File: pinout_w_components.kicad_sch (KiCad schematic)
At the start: 40 parts, among them J1 10155435-00011LF, U10 ESDS304DBVR, U11 ESD351DPYR, U12 TJA1051TK-3, U9 ESDS304DBVR

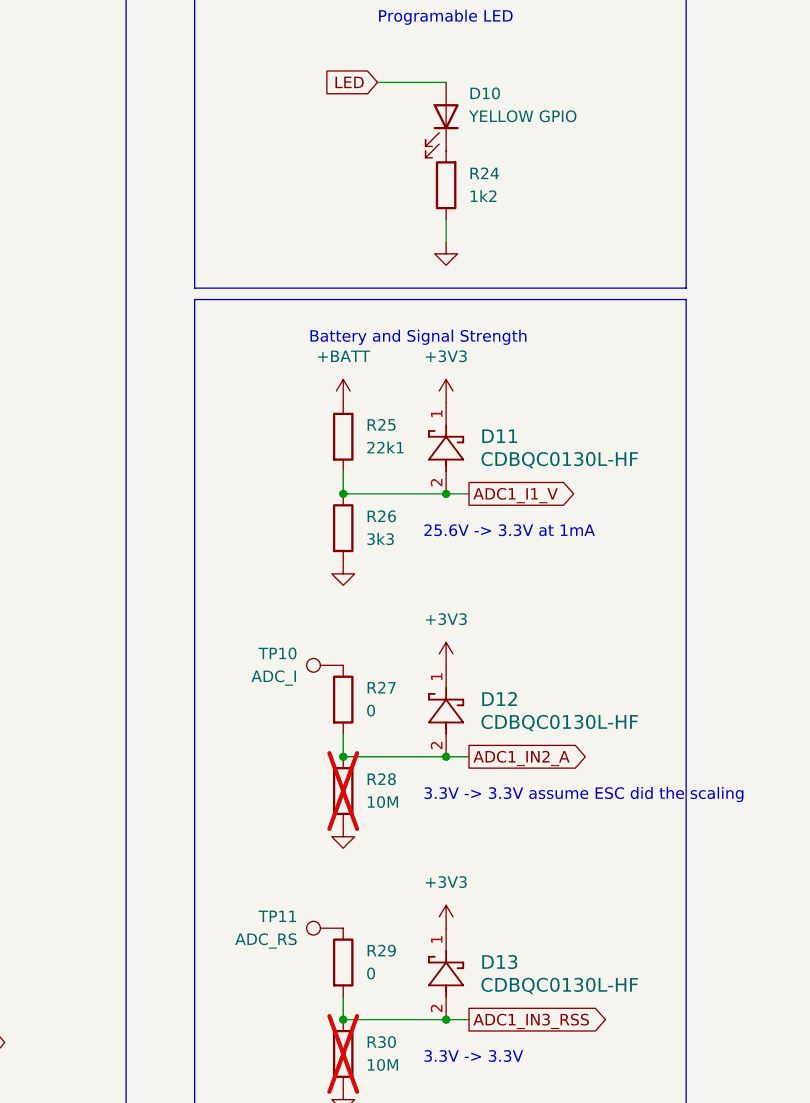
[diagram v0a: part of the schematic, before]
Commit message: replace flash memory with SD flash memory; move SPI2 terminations closer to source
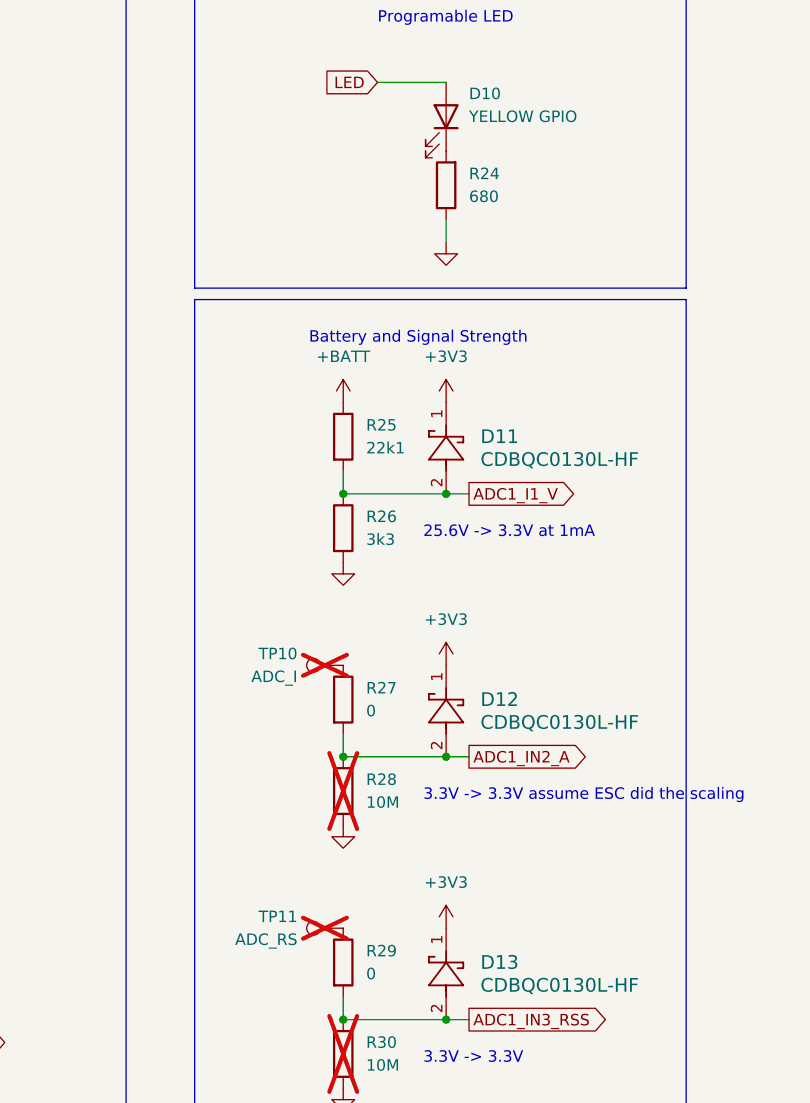
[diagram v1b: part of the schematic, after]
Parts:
- C40, C41: Part Number CC0402KRX7R7BB104 -> CC0402KRX5R8BB104; Voltage 16 -> 25
- C42: Manufactorer YAGEO -> Murata; Part Number CC0402JRX7R9BB472 -> GRM155R61H472KA01D; Voltage 16 -> 50
- C43, C44: Part Number CC0402JRX7R7BB101 -> CC0402JRNPO9BN101; Voltage 16 -> 50
- C51: Part Number GRM188C71C225KE11D -> GRM188R61E225KA12D; Voltage 16 -> 25
- R24: value 1k2 -> 680; Part Number RC0402FR-071K2L -> RC0402FR-07680RP
- R27: Part Number RP0402BRD0722K1L -> RC0402FR-070RL
- R28: Note (none) -> DNP; Part Number RT0402BRD073K3L -> RC0402JR-0710ML
- R29: Part Number RT0402BRD073K3L -> RC0402FR-070RL
- R30: Note (none) -> DNP
- TP10, TP11: now not fitted
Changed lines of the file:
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@@
 			)
 		)
-		(property "Part Number" "RT0402BRD073K3L"
+		(property "Part Number" "RC0402JR-0710ML"
+			(at 119.38 153.67 0)
+			(effects
+				(font
+					(size 1.27 1.27)
+				)
+				(hide yes)
+			)
+		)
+		(property "Note" "DNP"
 			(at 119.38 153.67 0)
 			(effects
@@
 			)
 		)
-		(property "Datasheet" "ESD351DPYR"
+		(property "Datasheet" "https://www.ti.com/general/docs/suppproductinfo.tsp?distId=10&gotoUrl=https%3A%2F%2Fwww.ti.com%2Flit%2Fgpn%2Fesd351"
 			(at 41.91 190.5 0)
 			(effects
@@
 			)
 		)
-		(property "Datasheet" "CDBQC0130L-HF"
+		(property "Datasheet" "https://www.comchiptech.com/admin/files/product/CDBQC0130L-HF%20RevB681116.pdf"
 			(at 130.81 179.07 0)
 			(effects
@@
 			)
 		)
-		(property "Part Number" "CC0402KRX7R7BB104"
+		(property "Part Number" "CC0402KRX5R8BB104"
 			(at 163.83 48.26 0)
 			(effects
@@
 			)
 		)
-		(property "Voltage" "16"
+		(property "Voltage" "25"
 			(at 163.83 48.26 0)
 			(effects
@@
 			)
 		)
-		(property "Part Number" "CC0402KRX7R7BB104"
+		(property "Part Number" "CC0402KRX5R8BB104"
 			(at 220.98 27.94 0)
 			(effects
@@
 			)
 		)
-		(property "Voltage" "16"
+		(property "Voltage" "25"
 			(at 220.98 27.94 0)
 			(effects
@@
 			)
 		)
-		(property "Part Number" "RP0402BRD0722K1L"
+		(property "Part Number" "RC0402FR-070RL"
 			(at 119.38 143.51 0)
 			(effects
@@
 			)
 		)
-		(property "Datasheet" "ESDS304DBVR"
+		(property "Datasheet" "https://www.ti.com/lit/ds/symlink/esds302.pdf?HQS=dis-dk-null-digikeymode-dsf-pf-null-wwe&ts=1721661223795&ref_url=https%253A%252F%252Ficqqg.com%252F"
 			(at 48.26 135.89 0)
 			(effects
@@
 			)
 		)
-		(property "Datasheet" "ESDS304DBVR"
+		(property "Datasheet" "https://www.ti.com/lit/ds/symlink/esds302.pdf?HQS=dis-dk-null-digikeymode-dsf-pf-null-wwe&ts=1721661223795&ref_url=https%253A%252F%252Ficqqg.com%252F"
 			(at 48.26 54.61 0)
 			(effects
@@
 			)
 		)
-		(property "Part Number" "CC0402JRX7R7BB101"
+		(property "Part Number" "CC0402JRNPO9BN101"
 			(at 209.55 50.8 0)
 			(effects
@@
 			)
 		)
-		(property "Voltage" "16"
+		(property "Voltage" "50"
 			(at 209.55 50.8 0)
 			(effects
@@
 			)
 		)
+		(property "Note" "DNP"
+			(at 119.38 182.88 0)
+			(effects
+				(font
+					(size 1.27 1.27)
+				)
+				(hide yes)
+			)
+		)
 		(pin "1"
 		)
@@
 			)
 		)
-		(property "Datasheet" "CDBQC0130L-HF"
+		(property "Datasheet" "https://www.comchiptech.com/admin/files/product/CDBQC0130L-HF%20RevB681116.pdf"
 			(at 130.81 120.65 0)
 			(effects
@@
 			)
 		)
-		(property "Manufactorer" "YAGEO"
+		(property "Manufactorer" "Murata"
 			(at 234.95 41.91 0)
 			(effects
@@
 			)
 		)
-		(property "Part Number" "CC0402JRX7R9BB472"
+		(property "Part Number" "GRM155R61H472KA01D "
 			(at 234.95 41.91 0)
 			(effects
@@
 			)
 		)
-		(property "Voltage" "16"
+		(property "Voltage" "50"
 			(at 234.95 41.91 0)
 			(effects
@@
 		(in_bom yes)
 		(on_board yes)
-		(dnp no)
+		(dnp yes)
 		(property "Reference" "TP11"
 			(at 114.3 167.64 90)
@@
 		(fields_autoplaced yes)
 		(property "Reference" "R24"
-			(at 133.35 85.09 0)
+			(at 133.35 85.0899 0)
 			(effects
 				(font
@@
 			)
 		)
-		(property "Value" "1k2"
-			(at 133.35 87.63 0)
+		(property "Value" "680"
+			(at 133.35 87.6299 0)
 			(effects
 				(font
@@
 			)
 		)
-		(property "Part Number" "RC0402FR-071K2L"
+		(property "Part Number" "RC0402FR-07680RP"
 			(at 130.81 86.36 0)
 			(effects
@@
 			)
 		)
-		(property "Part Number" "CC0402JRX7R7BB101"
+		(property "Part Number" "CC0402JRNPO9BN101"
 			(at 217.17 50.8 0)
 			(effects
@@
 			)
 		)
-		(property "Voltage" "16"
+		(property "Voltage" "50"
 			(at 217.17 50.8 0)
 			(effects
@@
 			)
 		)
-		(property "Datasheet" ""
+		(property "Datasheet" "https://cdn.amphenol-cs.com/media/wysiwyg/files/documentation/datasheet/inputoutput/io_usb_type_c_connector_cable.pdf"
 			(at 208.28 90.17 0)
 			(effects
@@
 			)
 		)
-		(property "Part Number" "RT0402BRD073K3L"
+		(property "Part Number" "RC0402FR-070RL"
 			(at 119.38 172.72 0)
 			(effects
@@
 			)
 		)
-		(property "Voltage" "16"
+		(property "Voltage" "25"
 			(at 226.06 27.94 0)
 			(effects
@@
 			)
 		)
-		(property "Part Number" "GRM188C71C225KE11D"
+		(property "Part Number" "GRM188R61E225KA12D"
 			(at 226.06 27.94 0)
 			(effects
@@
 		(in_bom yes)
 		(on_board yes)
-		(dnp no)
+		(dnp yes)
 		(property "Reference" "TP10"
 			(at 114.3 138.43 90)
@@
 			)
 		)
-		(property "Datasheet" "~"
+		(property "Datasheet" "https://optoelectronics.liteon.com/upload/download/DS22-2000-222/LTST-C191KFKT.pdf"
 			(at 130.81 78.74 0)
 			(effects
@@
 			)
 		)
-		(property "Datasheet" "CDBQC0130L-HF"
+		(property "Datasheet" "https://www.comchiptech.com/admin/files/product/CDBQC0130L-HF%20RevB681116.pdf"
 			(at 130.81 149.86 0)
 			(effects

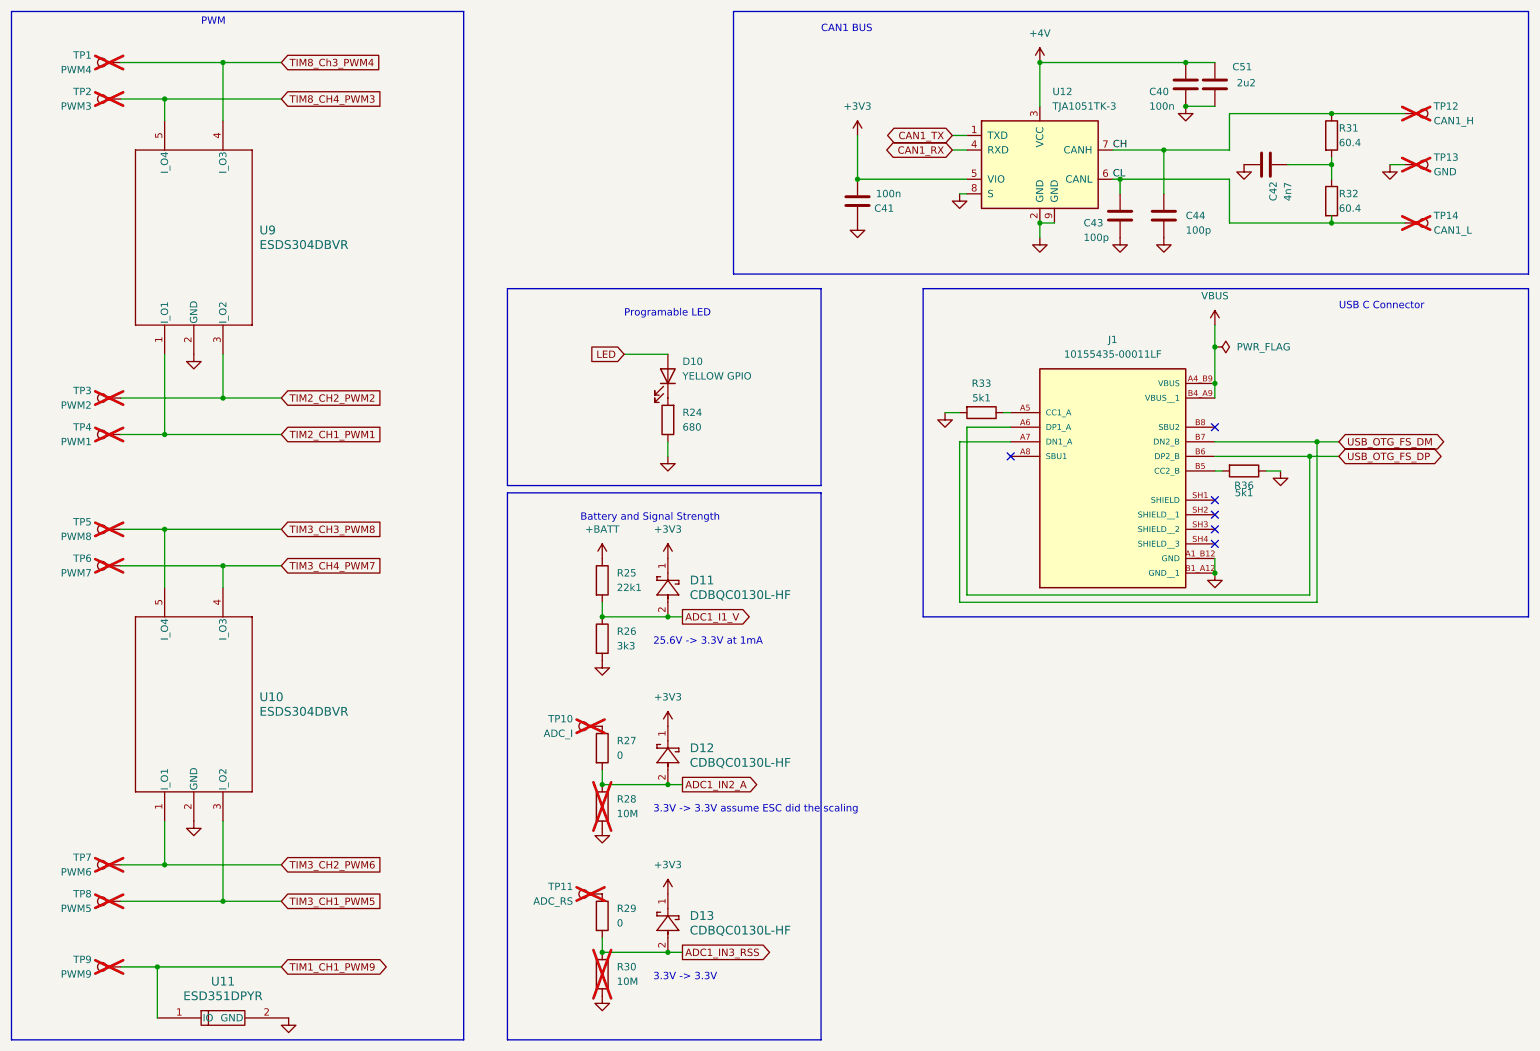
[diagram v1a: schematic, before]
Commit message: relabel components by sheet and block
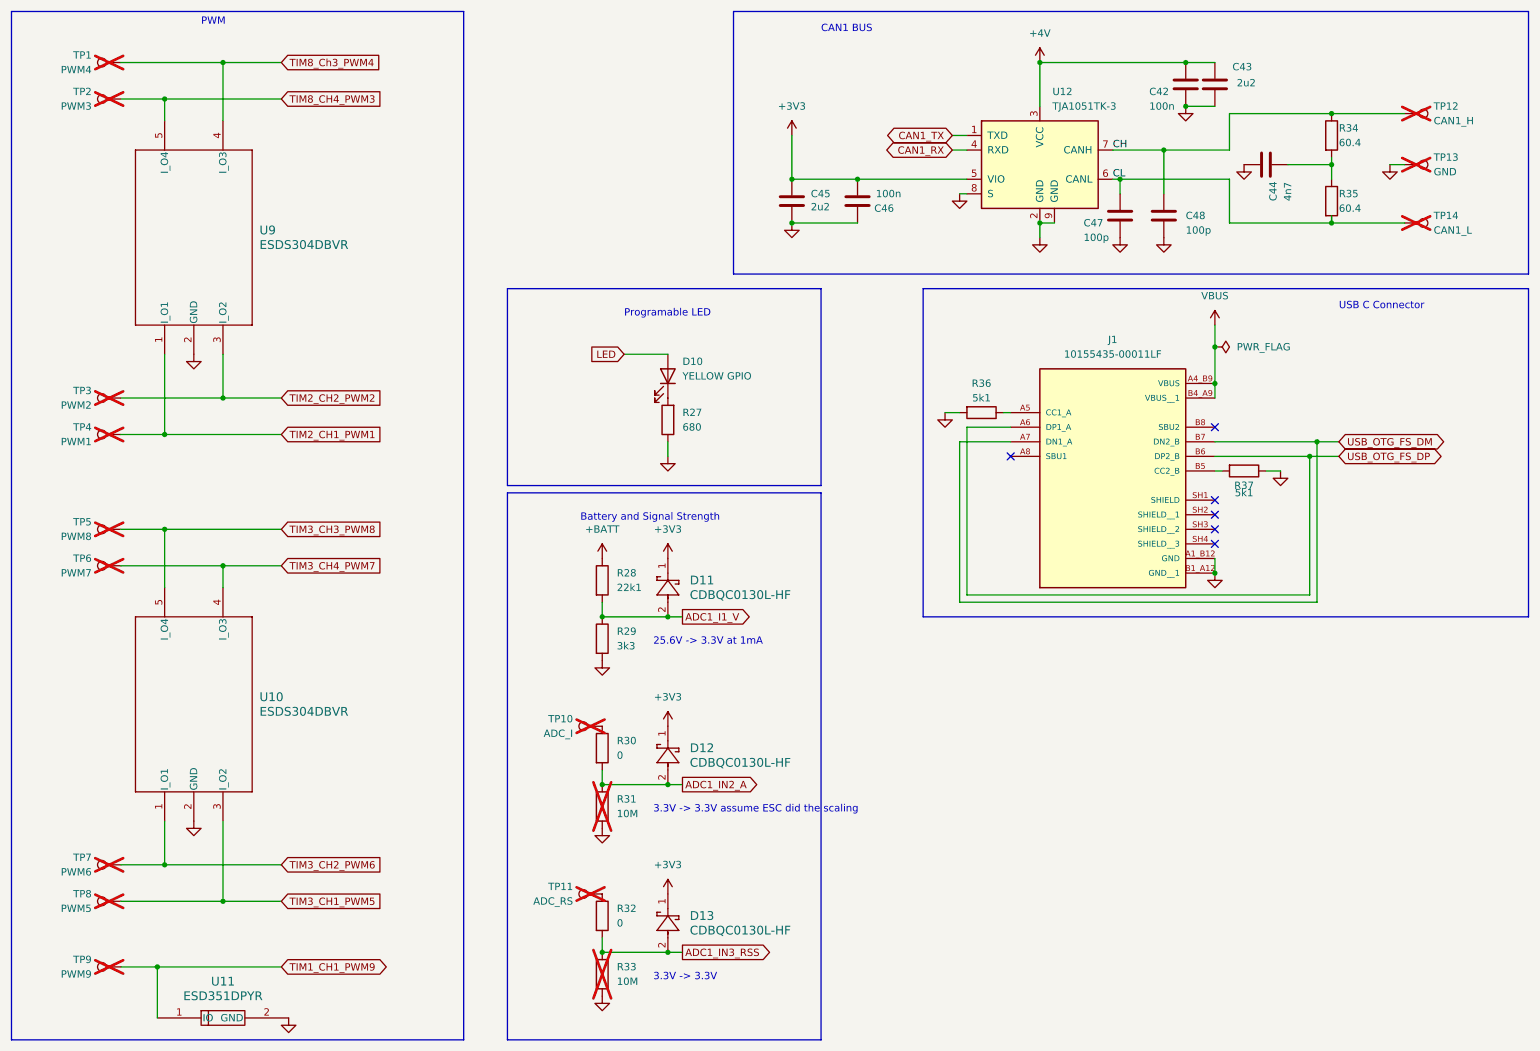
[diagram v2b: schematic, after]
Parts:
- added C45: 2u2, Capacitor_SMD:C_0603_1608Metric, symbol Device:C
- R28: renamed from R25; Part Number RP0402BRD0722K1L -> RT0402BRD0722K1L
- renumbered C40 to C42, C51 to C43, C42 to C44, C41 to C46, C43 to C47, C44 to C48, R24 to R27, R26 to R29, R27 to R30, R28 to R31, R29 to R32, R30 to R33, R31 to R34, R32 to R35, R33 to R36, R36 to R37
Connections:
- net +3V3: now also C45.1
- net GND: now also C45.2

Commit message: add more gerber files to .gitignore
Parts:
- D10: value YELLOW GPIO -> ORANGE GPIO
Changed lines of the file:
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@@
 			)
 		)
-		(property "Value" "YELLOW GPIO"
+		(property "Value" "ORANGE GPIO"
 			(at 133.35 78.74 90)
 			(effects
